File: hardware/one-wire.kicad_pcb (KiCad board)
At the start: 2 copper layers, 30 x 30 mm, 31 parts, among them P1 CON-SENSOR2, P2 DEBUG, P3 BOOT, P4 CONN_02X03, P5 CONN_01X03, U1 XMC13XX24, U2 NC7WZ07, U3 DRILL, U4 DRILL, U5 DRILL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

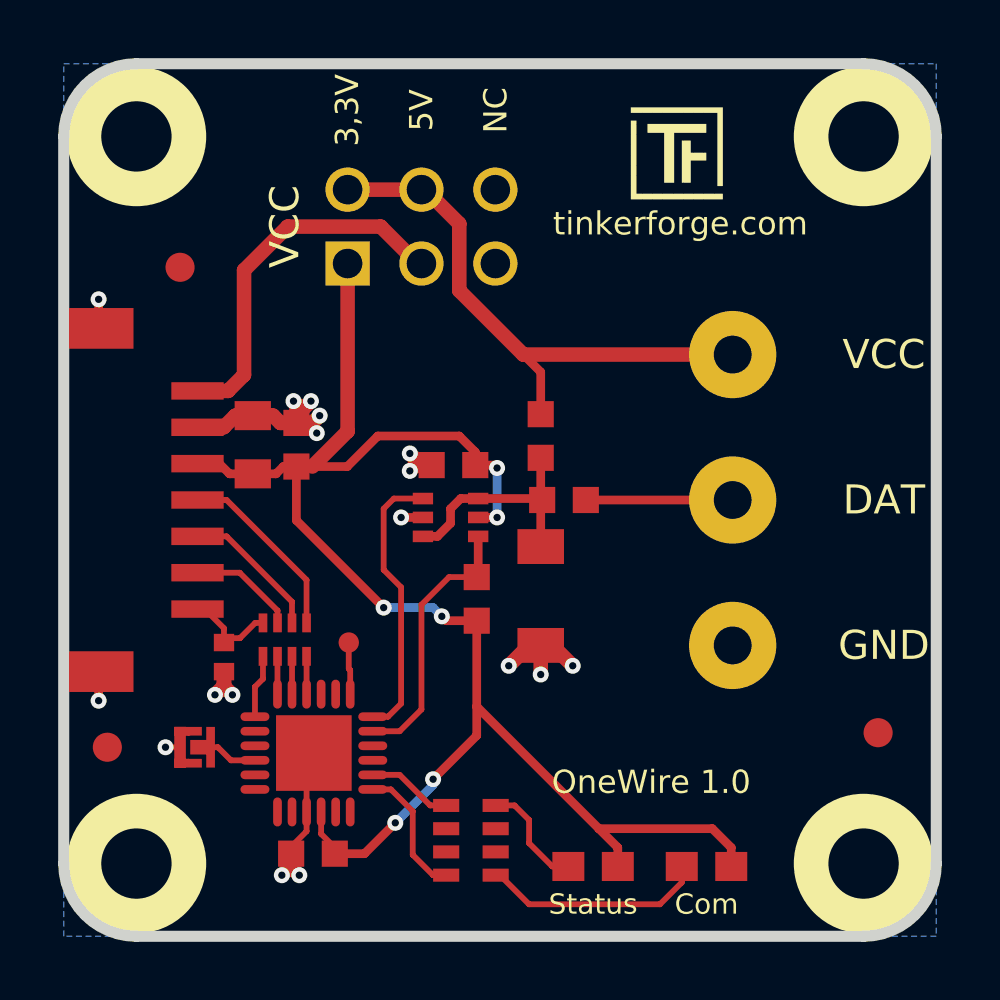
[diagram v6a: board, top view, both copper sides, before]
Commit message: increase hardware version to 1.1
* previous fixed (rx,tx moved) will be used
* add version detection pins (gnd)
* increase version number
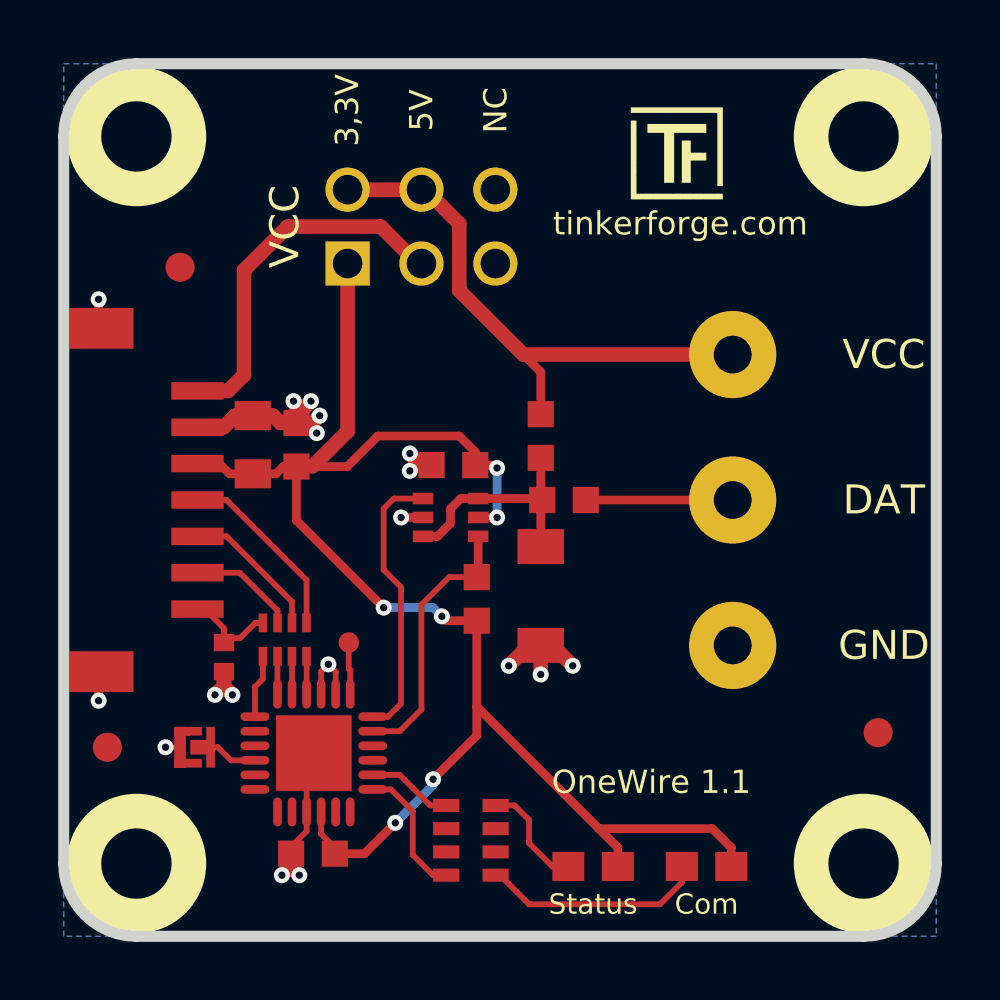
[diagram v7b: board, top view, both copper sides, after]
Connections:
- P1 pad 1: (no net) -> +5V
- P4 pad 2: Net-(P4-Pad2) -> VCC
- P4 pad 3: (no net) -> +5V
- P4 pad 4: Net-(P4-Pad2) -> VCC
- P5 pad 1: (no net) -> VCC
- R2 pad 1: (no net) -> VCC
- U1 pad 20: (no net) -> GND
- U1 pad 21: (no net) -> GND
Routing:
- net VCC: track 0.00 -> 19.2 mm
- net Net-(P4-Pad2): track 19.2 -> 0.00 mm
- net +5V: track 0.00 -> 12.7 mm
- net (no net): track 12.7 -> 0.00 mm
- net GND: track 29.0 -> 31.2 mm, vias 17 -> 18
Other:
- board text added: "OneWire 1.1"
- board text removed: "OneWire 1.0"
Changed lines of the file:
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@@
     (thickness 1.6)
     (drawings 20)
-    (tracks 205)
+    (tracks 210)
     (zones 0)
     (modules 31)
-    (nets 22)
+    (nets 23)
   )
   (page A4)
@@
   (net 19 "Net-(RP2-Pad5)")
   (net 20 "Net-(RP2-Pad8)")
-  (net 21 "Net-(P4-Pad2)")
+  (net 21 +5V)
+  (net 22 VCC)
   (net_class Default "This is the default net class."
     (clearance 0.15)
@@
     (uvia_dia 0.3)
     (uvia_drill 0.1)
+    (add_net +5V)
     (add_net 3V3)
     (add_net DAT)
@@
     (add_net "Net-(P2-Pad1)")
     (add_net "Net-(P3-Pad2)")
-    (add_net "Net-(P4-Pad2)")
     (add_net "Net-(RP2-Pad5)")
     (add_net "Net-(RP2-Pad8)")
@@
     (add_net S-MOSI)
     (add_net TX)
+    (add_net VCC)
   )
   (module kicad-libraries:Logo_CoMCU (layer B.Cu)
@@
     (pad 19 smd oval (at 1.25 -2.025 90) (size 1 0.3) (layers F.Cu F.Paste F.Mask)
       (net 14 "Net-(P2-Pad1)"))
-    (pad 20 smd oval (at 0.75 -2.025 90) (size 1 0.3) (layers F.Cu F.Paste F.Mask))
-    (pad 21 smd oval (at 0.25 -2.025 90) (size 1 0.3) (layers F.Cu F.Paste F.Mask))
+    (pad 20 smd oval (at 0.75 -2.025 90) (size 1 0.3) (layers F.Cu F.Paste F.Mask)
+      (net 1 GND))
+    (pad 21 smd oval (at 0.25 -2.025 90) (size 1 0.3) (layers F.Cu F.Paste F.Mask)
+      (net 1 GND))
     (pad 22 smd oval (at -0.25 -2.025 90) (size 1 0.3) (layers F.Cu F.Paste F.Mask)
       (net 3 S-CS))
@@
     (fp_line (start 7.50126 4.0005) (end 7.50126 -3.60172) (layer F.Fab) (width 0.01))
     (fp_line (start -7.50126 -3.60172) (end -7.50126 4.0005) (layer F.Fab) (width 0.01))
-    (pad 1 thru_hole circle (at -5 0 270) (size 2.99974 2.99974) (drill 1.30048) (layers *.Cu *.Mask F.SilkS))
+    (pad 1 thru_hole circle (at -5 0 270) (size 2.99974 2.99974) (drill 1.30048) (layers *.Cu *.Mask F.SilkS)
+      (net 22 VCC))
     (pad 2 thru_hole circle (at 0 0 270) (size 2.99974 2.99974) (drill 1.30048) (layers *.Cu *.Mask F.SilkS)
       (net 9 DAT))
@@
     (fp_line (start 6 -4.3) (end -6 -4.3) (layer F.Fab) (width 0.05))
     (fp_line (start -6 -4.3) (end -6 -0.25) (layer F.Fab) (width 0.05))
-    (pad 1 smd rect (at -3.75 -4.6 270) (size 0.6 1.8) (layers F.Cu F.Paste F.Mask))
+    (pad 1 smd rect (at -3.75 -4.6 270) (size 0.6 1.8) (layers F.Cu F.Paste F.Mask)
+      (net 21 +5V))
     (pad 2 smd rect (at -2.5 -4.6 270) (size 0.6 1.8) (layers F.Cu F.Paste F.Mask)
       (net 1 GND))
@@
       (net 6 3V3))
     (pad 2 thru_hole circle (at -2.54 -1.27) (size 1.524 1.524) (drill 1.016) (layers *.Cu *.Mask F.SilkS)
-      (net 21 "Net-(P4-Pad2)"))
-    (pad 3 thru_hole circle (at 0 1.27) (size 1.524 1.524) (drill 1.016) (layers *.Cu *.Mask F.SilkS))
+      (net 22 VCC))
+    (pad 3 thru_hole circle (at 0 1.27) (size 1.524 1.524) (drill 1.016) (layers *.Cu *.Mask F.SilkS)
+      (net 21 +5V))
     (pad 4 thru_hole circle (at 0 -1.27) (size 1.524 1.524) (drill 1.016) (layers *.Cu *.Mask F.SilkS)
-      (net 21 "Net-(P4-Pad2)"))
+      (net 22 VCC))
     (pad 5 thru_hole circle (at 2.54 1.27) (size 1.524 1.524) (drill 1.016) (layers *.Cu *.Mask F.SilkS))
     (pad 6 thru_hole circle (at 2.54 -1.27) (size 1.524 1.524) (drill 1.016) (layers *.Cu *.Mask F.SilkS))
@@
     (fp_line (start 1.45034 0.65024) (end -1.45034 0.65024) (layer F.Fab) (width 0.001))
     (fp_line (start -1.45034 0.65024) (end -1.45034 -0.65024) (layer F.Fab) (width 0.001))
-    (pad 1 smd rect (at -0.75 0 270) (size 0.9 0.9) (layers F.Cu F.Paste F.Mask))
+    (pad 1 smd rect (at -0.75 0 270) (size 0.9 0.9) (layers F.Cu F.Paste F.Mask)
+      (net 22 VCC))
     (pad 2 smd rect (at 0.75 0 270) (size 0.9 0.9) (layers F.Cu F.Paste F.Mask)
       (net 18 "Net-(D2-Pad2)"))
@@
     (effects (font (size 0.8 0.8) (thickness 0.15)))
   )
-  (gr_text "OneWire 1.0" (at 152.5 134.4) (layer F.SilkS)
+  (gr_text "OneWire 1.1" (at 152.5 134.4) (layer F.SilkS)
     (effects (font (size 0.8 0.8) (thickness 0.15)))
   )
@@
     (effects (font (size 0.8 0.8) (thickness 0.15)))
   )
-  (segment (start 144.6 116.57) (end 144.47 116.57) (width 0.5) (layer F.Cu) (net 0))
-  (segment (start 144.47 116.57) (end 143.2 115.3) (width 0.5) (layer F.Cu) (net 0))
-  (segment (start 143.2 115.3) (end 140 115.3) (width 0.5) (layer F.Cu) (net 0))
-  (segment (start 140 115.3) (end 138.5 116.8) (width 0.5) (layer F.Cu) (net 0))
-  (segment (start 138.5 116.8) (end 138.5 120.4) (width 0.5) (layer F.Cu) (net 0))
-  (segment (start 138.5 120.4) (end 137.95 120.95) (width 0.5) (layer F.Cu) (net 0))
-  (segment (start 137.95 120.95) (end 136.9 120.95) (width 0.5) (layer F.Cu) (net 0))
   (segment (start 136.3 133.2) (end 136.3 133.6) (width 0.2) (layer F.Cu) (net 1))
   (segment (start 136.3 133.6) (end 136.4 133.7) (width 0.2) (layer F.Cu) (net 1))
@@
   (segment (start 140.15 136.59) (end 140.65 136.09) (width 0.2) (layer F.Cu) (net 1))
   (segment (start 140.65 136.09) (end 140.65 135.425) (width 0.2) (layer F.Cu) (net 1))
+  (segment (start 141.65 131.375) (end 141.65 130.6) (width 0.2) (layer F.Cu) (net 1) (status 400000))
+  (segment (start 141.15 130.6) (end 141.4 130.35) (width 0.2) (layer F.Cu) (net 1))
+  (segment (start 141.15 130.6) (end 141.15 131.375) (width 0.2) (layer F.Cu) (net 1) (status 800000))
+  (segment (start 141.65 130.6) (end 141.4 130.35) (width 0.2) (layer F.Cu) (net 1))
+  (via (at 141.4 130.35) (size 0.55) (drill 0.25) (layers F.Cu B.Cu) (net 1))
   (segment (start 139.1507 130.075) (end 139.1507 130.8493) (width 0.2) (layer F.Cu) (net 2))
   (segment (start 138.875 131.125) (end 138.875 132.15) (width 0.2) (layer F.Cu) (net 2))
@@
   (segment (start 144.90112 135.20112) (end 145.4491 135.20112) (width 0.2) (layer F.Cu) (net 20))
   (segment (start 143.85 134.15) (end 144.90112 135.20112) (width 0.2) (layer F.Cu) (net 20))
-  (segment (start 148.7 121.75) (end 148.7 120.3) (width 0.3) (layer F.Cu) (net 21))
-  (segment (start 148.7 120.3) (end 148.1 119.7) (width 0.3) (layer F.Cu) (net 21))
-  (segment (start 144.6 114.03) (end 142.06 114.03) (width 0.5) (layer F.Cu) (net 21))
-  (segment (start 155.3 119.7) (end 148.1 119.7) (width 0.5) (layer F.Cu) (net 21))
-  (segment (start 145.9 115.2) (end 144.73 114.03) (width 0.5) (layer F.Cu) (net 21))
-  (segment (start 145.9 117.5) (end 145.9 115.2) (width 0.5) (layer F.Cu) (net 21))
-  (segment (start 148.1 119.7) (end 145.9 117.5) (width 0.5) (layer F.Cu) (net 21))
-  (segment (start 144.73 114.03) (end 144.6 114.03) (width 0.5) (layer F.Cu) (net 21))
+  (segment (start 144.6 116.57) (end 144.47 116.57) (width 0.5) (layer F.Cu) (net 21))
+  (segment (start 144.47 116.57) (end 143.2 115.3) (width 0.5) (layer F.Cu) (net 21))
+  (segment (start 143.2 115.3) (end 140 115.3) (width 0.5) (layer F.Cu) (net 21))
+  (segment (start 140 115.3) (end 138.5 116.8) (width 0.5) (layer F.Cu) (net 21))
+  (segment (start 138.5 116.8) (end 138.5 120.4) (width 0.5) (layer F.Cu) (net 21))
+  (segment (start 138.5 120.4) (end 137.95 120.95) (width 0.5) (layer F.Cu) (net 21))
+  (segment (start 137.95 120.95) (end 136.9 120.95) (width 0.5) (layer F.Cu) (net 21))
+  (segment (start 148.7 121.75) (end 148.7 120.3) (width 0.3) (layer F.Cu) (net 22))
+  (segment (start 148.7 120.3) (end 148.1 119.7) (width 0.3) (layer F.Cu) (net 22))
+  (segment (start 144.6 114.03) (end 142.06 114.03) (width 0.5) (layer F.Cu) (net 22))
+  (segment (start 155.3 119.7) (end 148.1 119.7) (width 0.5) (layer F.Cu) (net 22))
+  (segment (start 145.9 115.2) (end 144.73 114.03) (width 0.5) (layer F.Cu) (net 22))
+  (segment (start 145.9 117.5) (end 145.9 115.2) (width 0.5) (layer F.Cu) (net 22))
+  (segment (start 148.1 119.7) (end 145.9 117.5) (width 0.5) (layer F.Cu) (net 22))
+  (segment (start 144.73 114.03) (end 144.6 114.03) (width 0.5) (layer F.Cu) (net 22))
   (zone (net 1) (net_name GND) (layer B.Cu) (hatch edge 0.508)
     (connect_pads yes (clearance 0.2))

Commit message: specify processor xmc1302
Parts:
- U1: value XMC13XX24 -> XMC1302
